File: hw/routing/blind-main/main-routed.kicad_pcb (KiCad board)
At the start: 4 copper layers, 54 x 71 mm, 196 parts

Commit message: Route local USB power and CC paths with isolated return checks
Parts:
- moved D5 32.2 mm to (122.1, 169.7), turned to 0 degrees
- moved R82 25.8 mm to (149.7, 160.4)
- moved R56 23.7 mm to (122.6, 160.6), turned to 180 degrees
- moved R65 23.1 mm to (122.6, 162.2), turned to 180 degrees
- moved C49 18.3 mm to (122.1, 166.0), turned to 90 degrees
- moved C50 17.5 mm to (127.7, 168.0), turned to 0 degrees
- moved C18 16.9 mm to (146.5, 171.7), turned to 180 degrees
- moved C48 15.1 mm to (135.5, 165.7), turned to 180 degrees
- moved D3 15.0 mm to (136.2, 170.1), turned to 180 degrees
- moved R2 14.0 mm to (141.6, 169.7)
- moved R52 12.8 mm to (127.7, 165.6)
- moved C12 12.0 mm to (139.1, 161.1)
- moved Q1 11.2 mm to (122.4, 158.1), turned to 0 degrees
- moved C10 9.23 mm to (126.0, 155.6)
- moved C51 6.57 mm to (135.5, 167.4), turned to 180 degrees
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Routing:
- net lv: track 46.2 -> 82.7 mm, vias 34 -> 45
- net raw-hv: track 0.00 -> 31.6 mm, vias 0 -> 5
- net CC2: track 0.00 -> 19.4 mm, vias 0 -> 2
- net connector-1: track 0.00 -> 18.7 mm, vias 0 -> 2
- net usb-output-hv: track 3.38 -> 17.7 mm, vias 0 -> 4
- net usb-2: track 0.00 -> 7.97 mm, vias 0 -> 2
- net c_vdd-1: track 0.00 -> 5.25 mm
- net efuse-1: track 0.00 -> 5.12 mm, vias 0 -> 2
- net c_1v2-1: track 0.00 -> 2.32 mm
- net DVDT: track 0.00 -> 2.18 mm
- net c_2v7-1: track 0.00 -> 2.03 mm
- net controller-1-2: track 0.00 -> 1.82 mm
- net controller-1-3: track 0.00 -> 1.82 mm
- net ILM: track 0.00 -> 1.37 mm

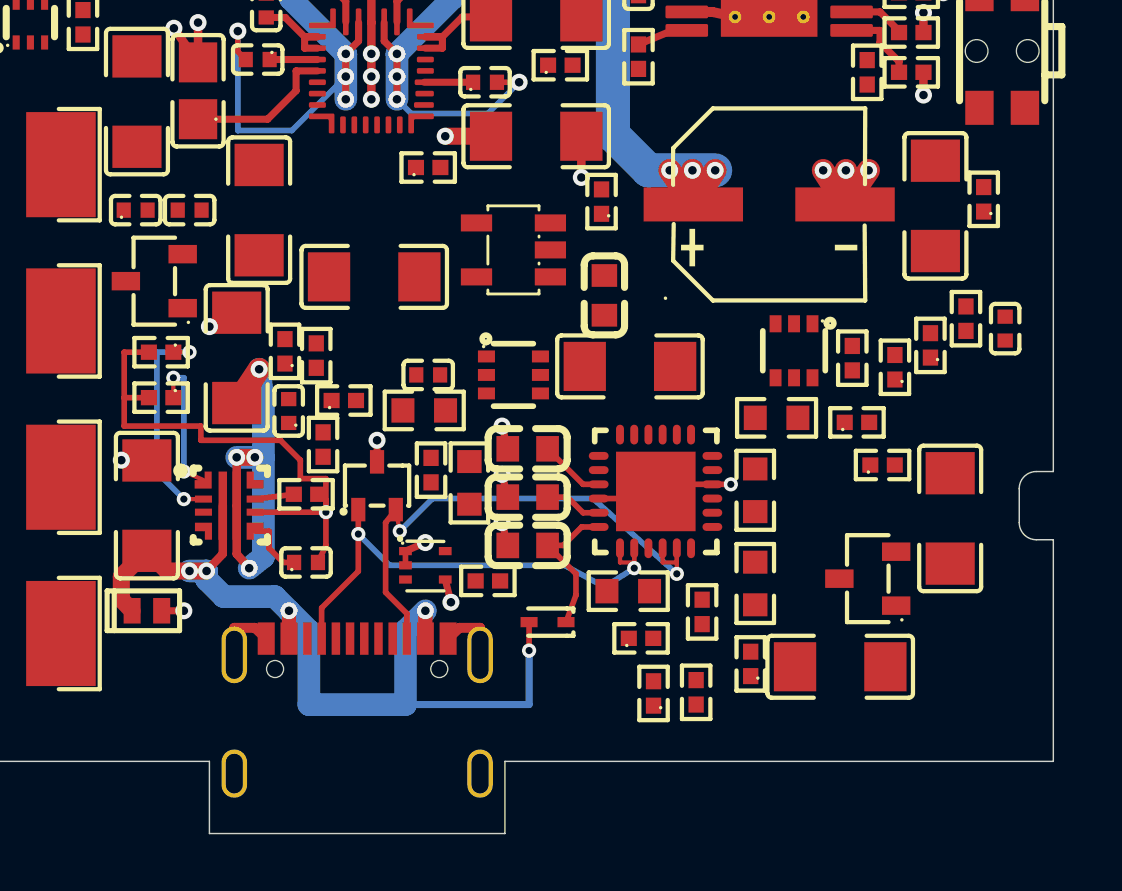
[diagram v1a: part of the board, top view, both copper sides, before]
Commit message: Connect USB enable, divider and discharge control chains
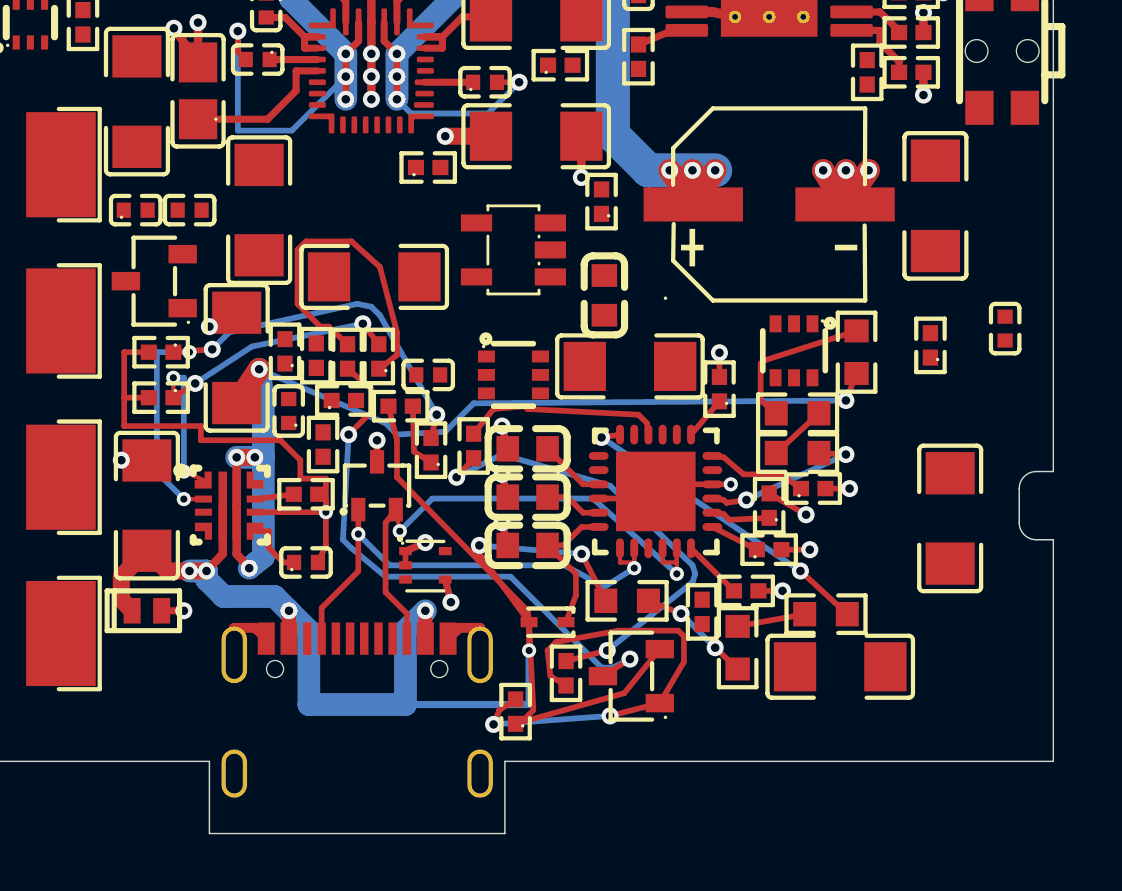
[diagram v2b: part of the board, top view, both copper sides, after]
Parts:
- moved R66 21.8 mm to (129.2, 160.8)
- moved R53 15.4 mm to (147.1, 160.6), turned to 90 degrees
- moved R57 14.5 mm to (131.0, 162.5), turned to 0 degrees
- moved R63 14.5 mm to (144.0, 167.6), turned to 0 degrees
- moved R50 13.7 mm to (133.6, 163.9)
- moved R67 13.5 mm to (130.3, 160.8), turned to 90 degrees
- moved R58 11.6 mm to (132.1, 164.1)
- moved R60 11.1 mm to (142.9, 171.0)
- moved R62 9.10 mm to (143.2, 169.0)
- moved Q3 9.00 mm to (139.2, 172.0)
- moved R49 8.58 mm to (136.8, 171.9)
- moved R51 8.44 mm to (135.1, 173.2)
- moved R64 6.58 mm to (144.0, 166.0)
- moved R48 4.98 mm to (142.2, 161.9), turned to 90 degrees
- moved R54 3.09 mm to (145.0, 162.8), turned to 0 degrees
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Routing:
- net raw-hv: track 31.6 -> 59.7 mm, vias 5 -> 7
- net usb-output-hv: track 17.7 -> 41.8 mm, vias 4 -> 5
- net C: track 0.00 -> 19.8 mm, vias 0 -> 2
- net r_base1-1: track 0.00 -> 16.6 mm, vias 0 -> 2
- net q_enable-1: track 0.00 -> 16.3 mm, vias 0 -> 2
- net usb-2: track 7.97 -> 20.6 mm, vias 2 -> 4
- net r_uv_top1-1: track 0.00 -> 11.6 mm
- net VBUS_VS_DISCH: track 0.00 -> 11.3 mm, vias 0 -> 2
- net efuse-1: track 5.12 -> 13.3 mm, vias 2 -> 4
- net VBUS_EN_SNK: track 0.00 -> 7.10 mm
- net DISCH: track 0.00 -> 6.05 mm, vias 0 -> 2
- net r_out_dis1-1: track 0.00 -> 5.59 mm
- net lv: track 82.7 -> 87.7 mm, vias 45 -> 50
- net r_raw_dis1-1: track 0.00 -> 4.02 mm, vias 0 -> 2
- net pd-1: track 0.00 -> 3.50 mm
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
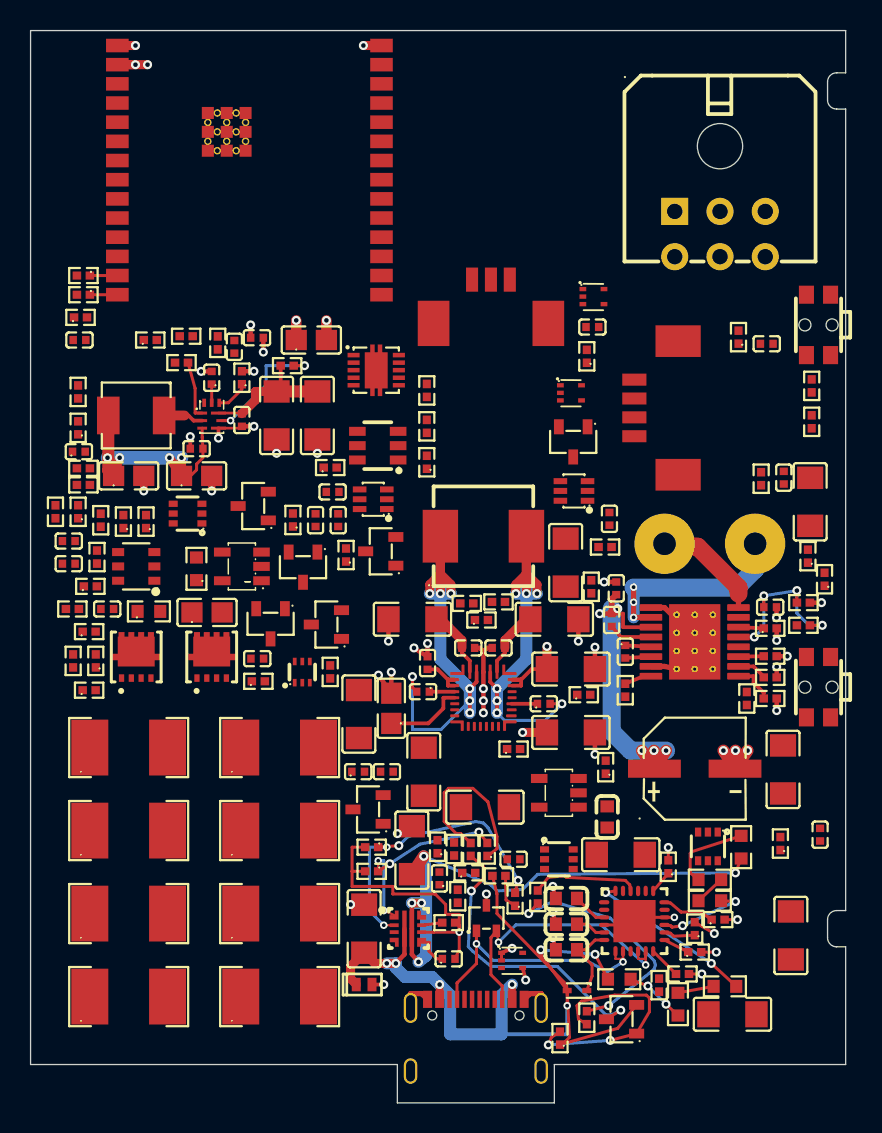
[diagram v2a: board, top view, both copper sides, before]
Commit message: Connect charger input and bulk capacitor distribution
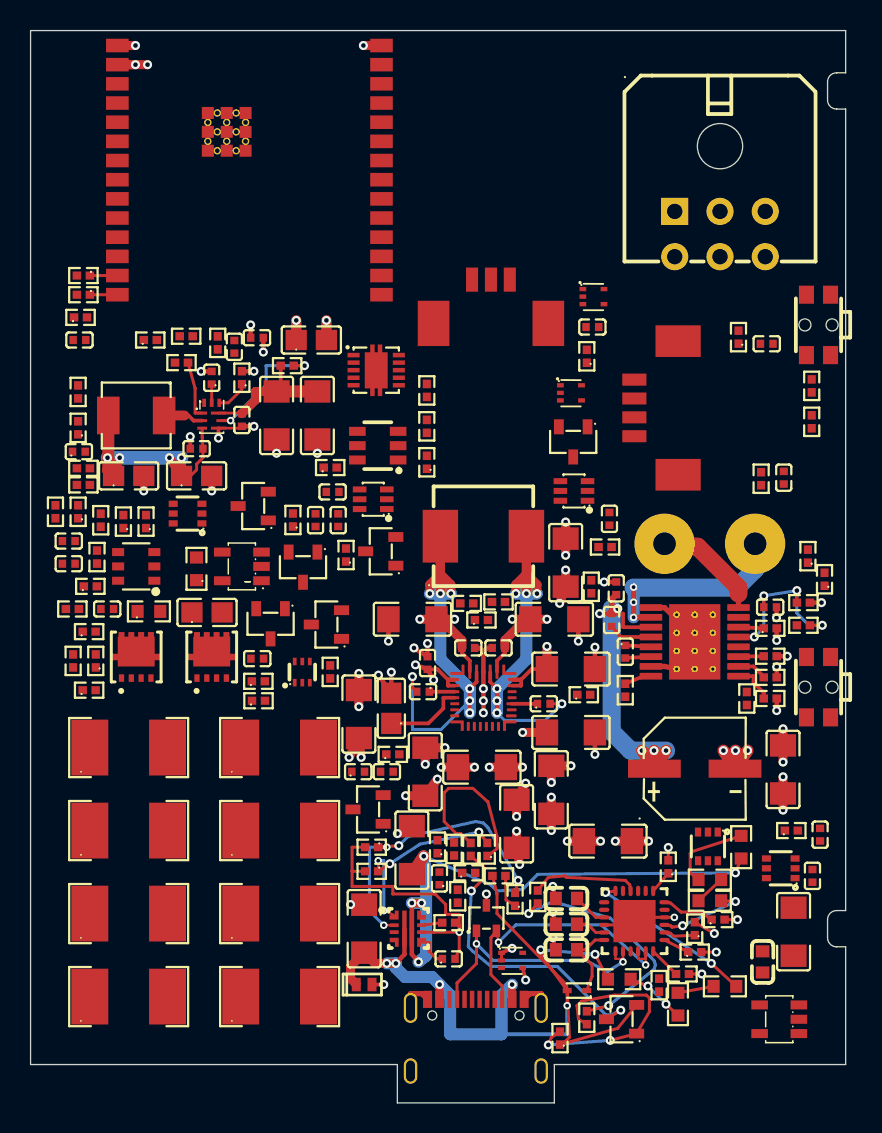
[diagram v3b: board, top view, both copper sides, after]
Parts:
- moved R82 35.8 mm to (115.1, 150.9), turned to 0 degrees
- moved C54 22.1 mm to (150.6, 166.2), turned to 90 degrees
- moved U13 20.9 mm to (149.6, 172.0)
- moved C52 19.8 mm to (151.8, 162.5), turned to 90 degrees
- moved C18 19.1 mm to (134.5, 156.8), turned to -90 degrees
- moved C17 16.7 mm to (135.4, 141.8)
- moved U12 14.7 mm to (149.7, 162.0), turned to 0 degrees
- moved C11 14.6 mm to (129.9, 155.3), turned to 0 degrees
- moved C53 14.1 mm to (148.5, 168.2)
- moved R68 13.0 mm to (150.4, 159.5), turned to 0 degrees
- moved C19 12.5 mm to (138.2, 160.2), turned to 0 degrees
- moved C20 11.0 mm to (149.8, 155.4)
- moved R5 8.01 mm to (124.0, 154.4)
- moved C12 7.20 mm to (132.2, 159.1), turned to -90 degrees
- moved C10 0.10 mm to (126.2, 155.6), turned to -90 degrees
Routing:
- net source-hv: track 13.9 -> 68.4 mm, vias 0 -> 10
- net c_pmid1-1: track 4.56 -> 37.9 mm, vias 0 -> 8
- net usb-output-hv: track 41.8 -> 66.5 mm, vias 5 -> 9
- net lv: track 87.7 -> 105.8 mm, vias 50 -> 66

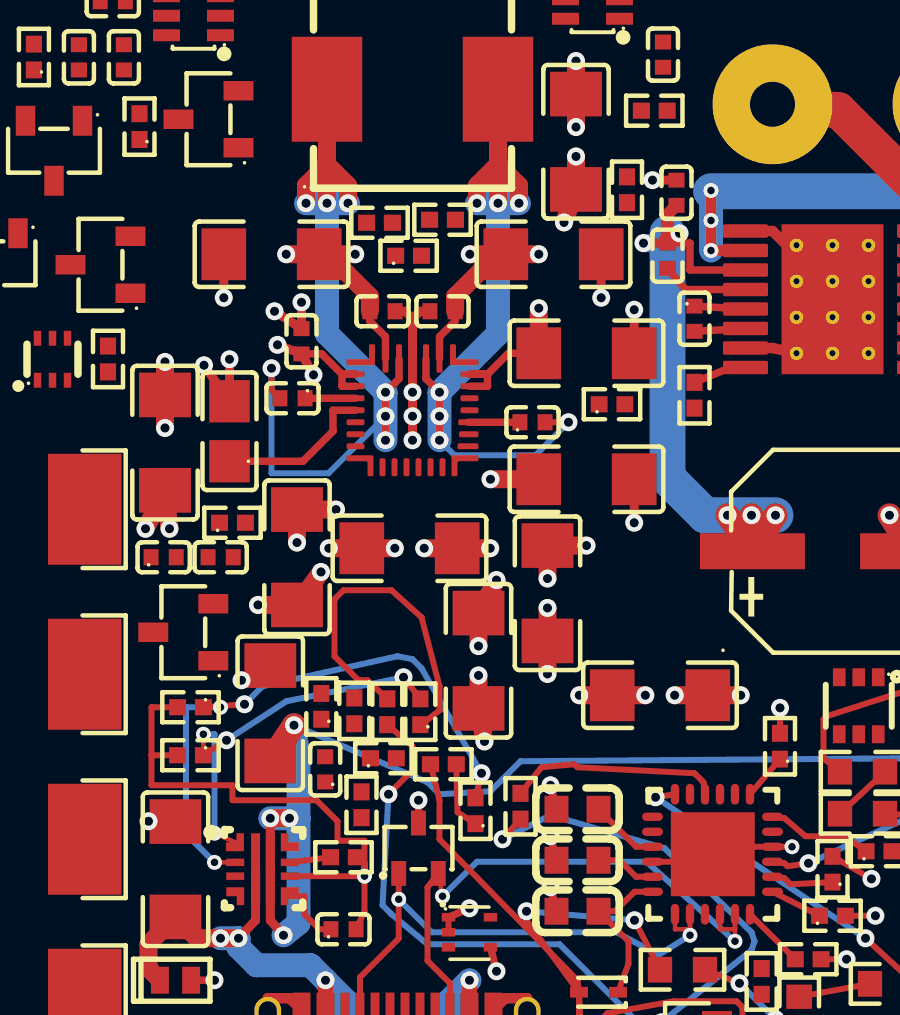
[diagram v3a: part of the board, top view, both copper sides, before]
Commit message: Route charger sensing and control networks with physical checks
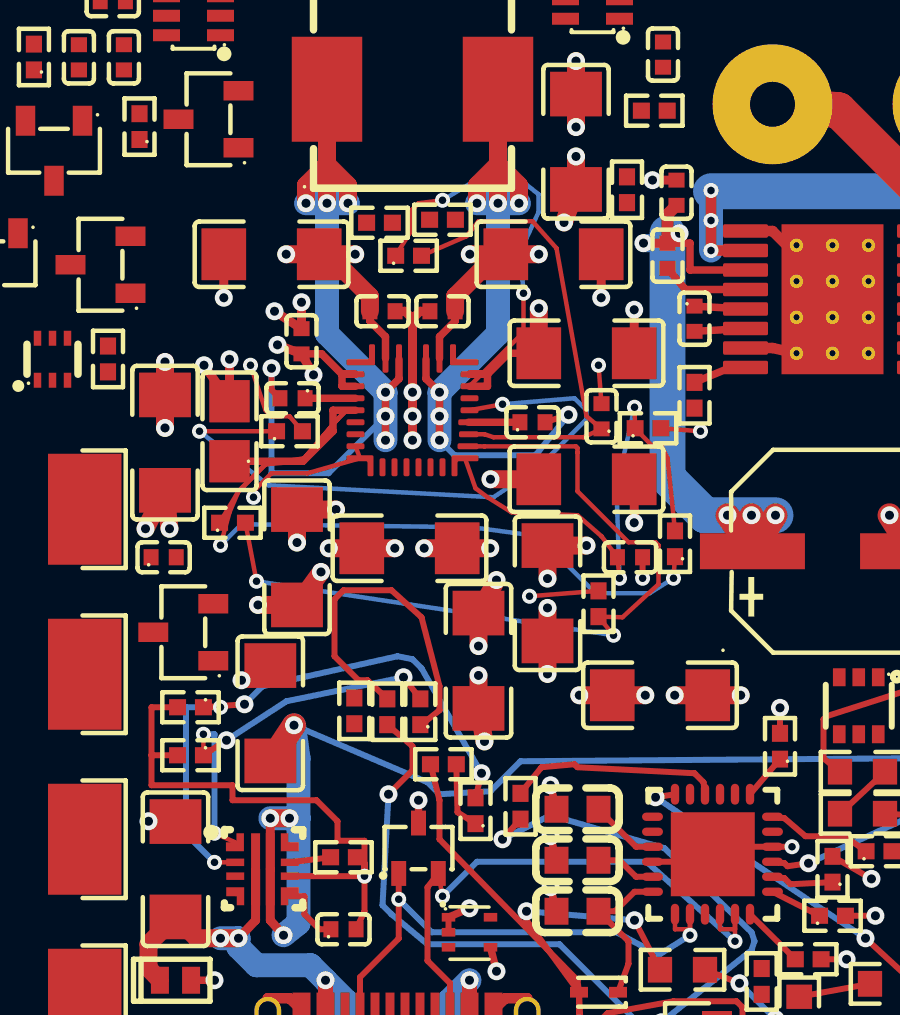
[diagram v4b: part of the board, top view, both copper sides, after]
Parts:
- moved C3 14.9 mm to (136.3, 150.9)
- moved C22 13.6 mm to (137.2, 155.6)
- moved R10 13.0 mm to (138.8, 155.2)
- moved R8 11.3 mm to (125.9, 151.4)
- moved R4 10.4 mm to (136.2, 157.2)
- moved R9 1.44 mm to (137.8, 151.3)
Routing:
- net c_regn-1: track 5.31 -> 35.6 mm, vias 0 -> 2
- net ILIM_HIZ: track 0.00 -> 27.1 mm, vias 0 -> 2
- net PROG: track 0.00 -> 21.5 mm, vias 0 -> 2
- net pack_ntc: track 0.00 -> 17.8 mm, vias 0 -> 2
- net BATP: track 0.00 -> 16.1 mm
- net hv: track 37.8 -> 51.3 mm, vias 7 -> 9
- net lv: track 105.8 -> 114.5 mm, vias 66 -> 71
- net usb-output-hv: track 66.5 -> 72.6 mm, vias 9 -> 10

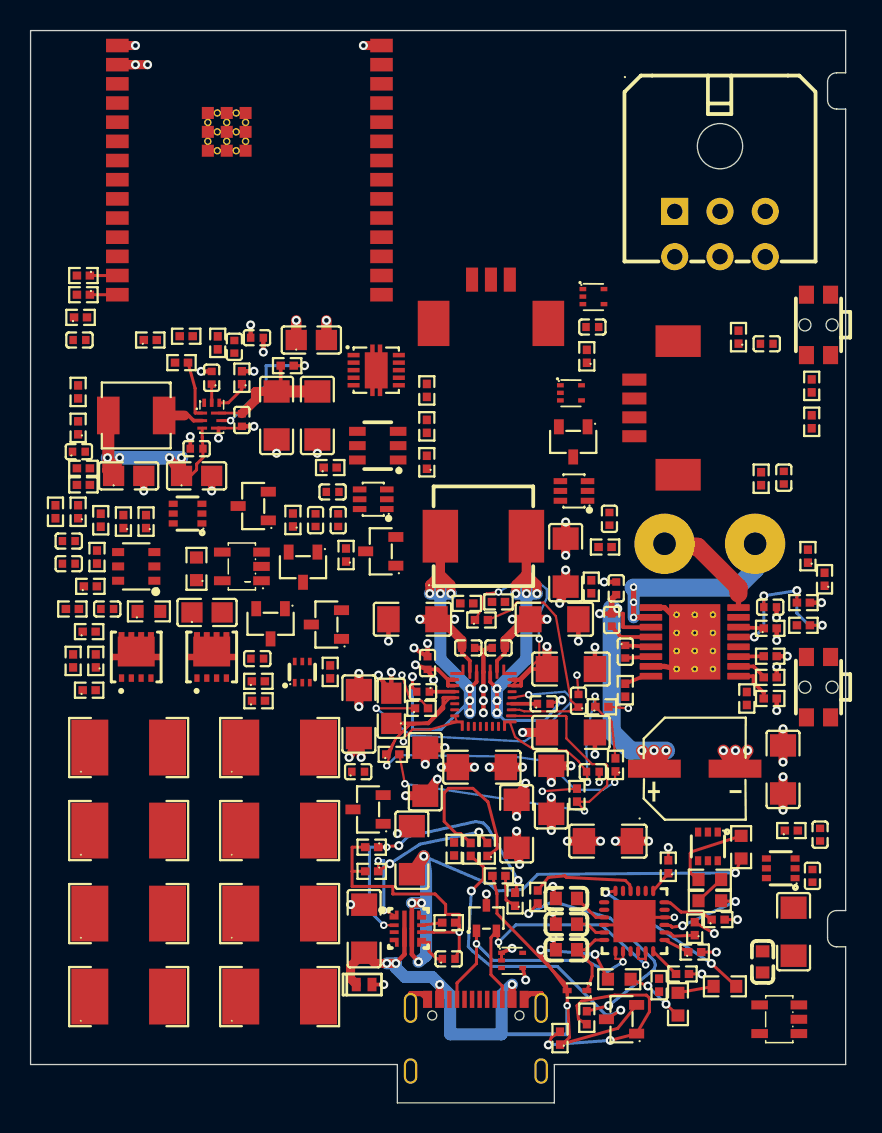
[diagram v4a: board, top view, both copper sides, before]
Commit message: Keep all main-board routing vias clear of solder lands
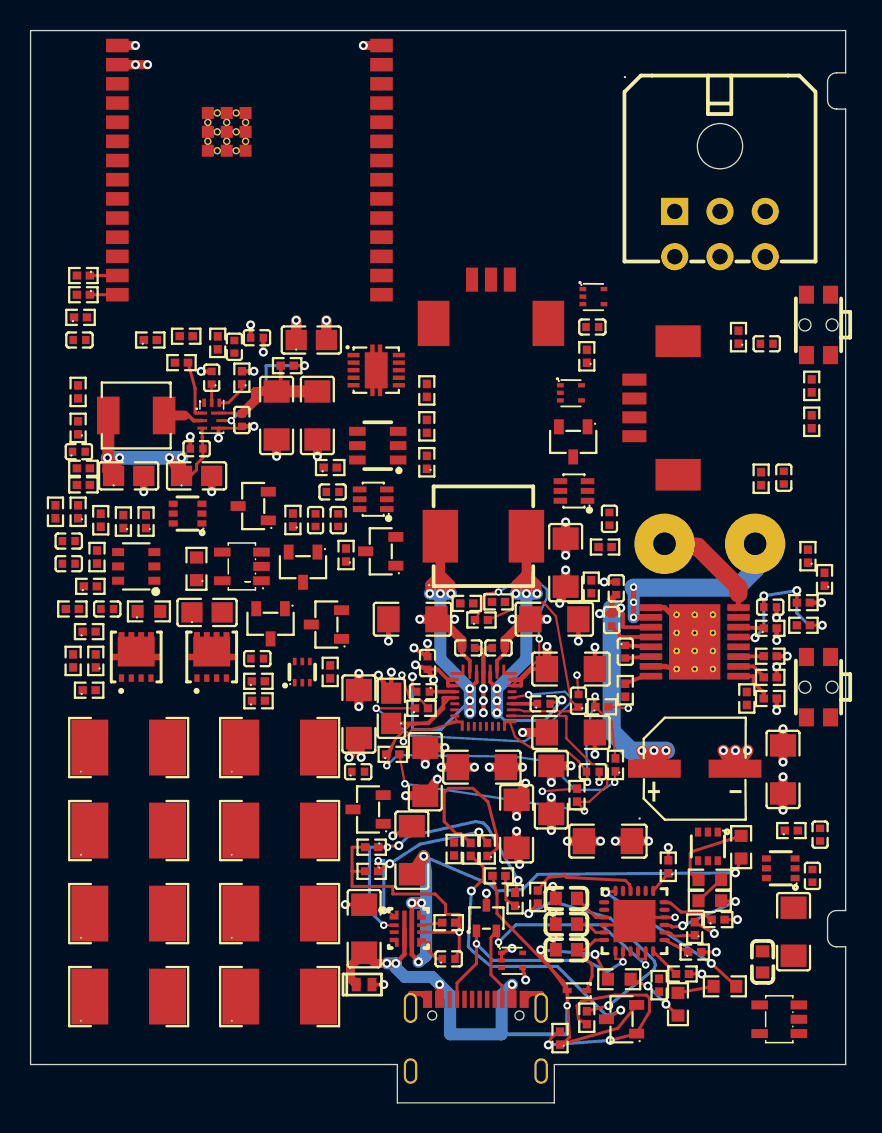
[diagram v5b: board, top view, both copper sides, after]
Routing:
- net lv: track 114.5 -> 116.9 mm
- net hv: track 51.3 -> 51.9 mm

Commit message: Route regenerative clamp with reproducible physical topology checks
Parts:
- moved R79 21.7 mm to (122.0, 146.0)
- moved R80 19.6 mm to (122.0, 144.0)
- moved C37 18.9 mm to (124.0, 143.8)
- moved C55 15.4 mm to (116.0, 149.1), turned to 90 degrees
- moved Q4 13.1 mm to (103.0, 148.0)
- moved R40 11.5 mm to (112.6, 138.8), turned to 90 degrees
- moved R41 10.7 mm to (113.8, 138.8)
- moved R75 9.62 mm to (101.8, 139.5), turned to -90 degrees
- moved R86 7.41 mm to (103.0, 144.8)
- moved R76 7.15 mm to (103.2, 139.5), turned to 90 degrees
- moved R85 6.48 mm to (106.0, 139.2), turned to 90 degrees
- moved Q5 6.26 mm to (109.8, 141.9), turned to 90 degrees
- moved R82 6.11 mm to (109.0, 151.2)
- moved R78 5.93 mm to (104.8, 144.8)
- moved R88 5.60 mm to (101.8, 145.0), turned to 90 degrees
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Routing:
- net hv: track 51.9 -> 183.7 mm, vias 9 -> 19
- net c_hot_filter-1: track 0.00 -> 49.3 mm, vias 0 -> 7
- net regen-2-1: track 0.00 -> 34.1 mm
- net lv: track 116.9 -> 150.4 mm, vias 71 -> 86
- net G: track 0.00 -> 23.1 mm, vias 0 -> 2
- net q_drive-1: track 0.00 -> 19.0 mm, vias 0 -> 4
- net thermal_ok: track 0.00 -> 18.1 mm
- net series_mid: track 0.00 -> 15.0 mm
- net PROG: track 21.5 -> 32.2 mm
- net OUTB: track 0.00 -> 10.1 mm
- net threshold: track 0.00 -> 9.83 mm, vias 0 -> 2
- net regen-2: track 0.00 -> 9.10 mm
- net thermal_gate: track 0.00 -> 8.85 mm
- net regen-2-2: track 0.00 -> 8.40 mm
- net pack_ntc: track 17.8 -> 25.0 mm
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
